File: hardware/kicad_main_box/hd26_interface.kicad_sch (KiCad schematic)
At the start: 1 part, among them J1 HD26_FEMALE

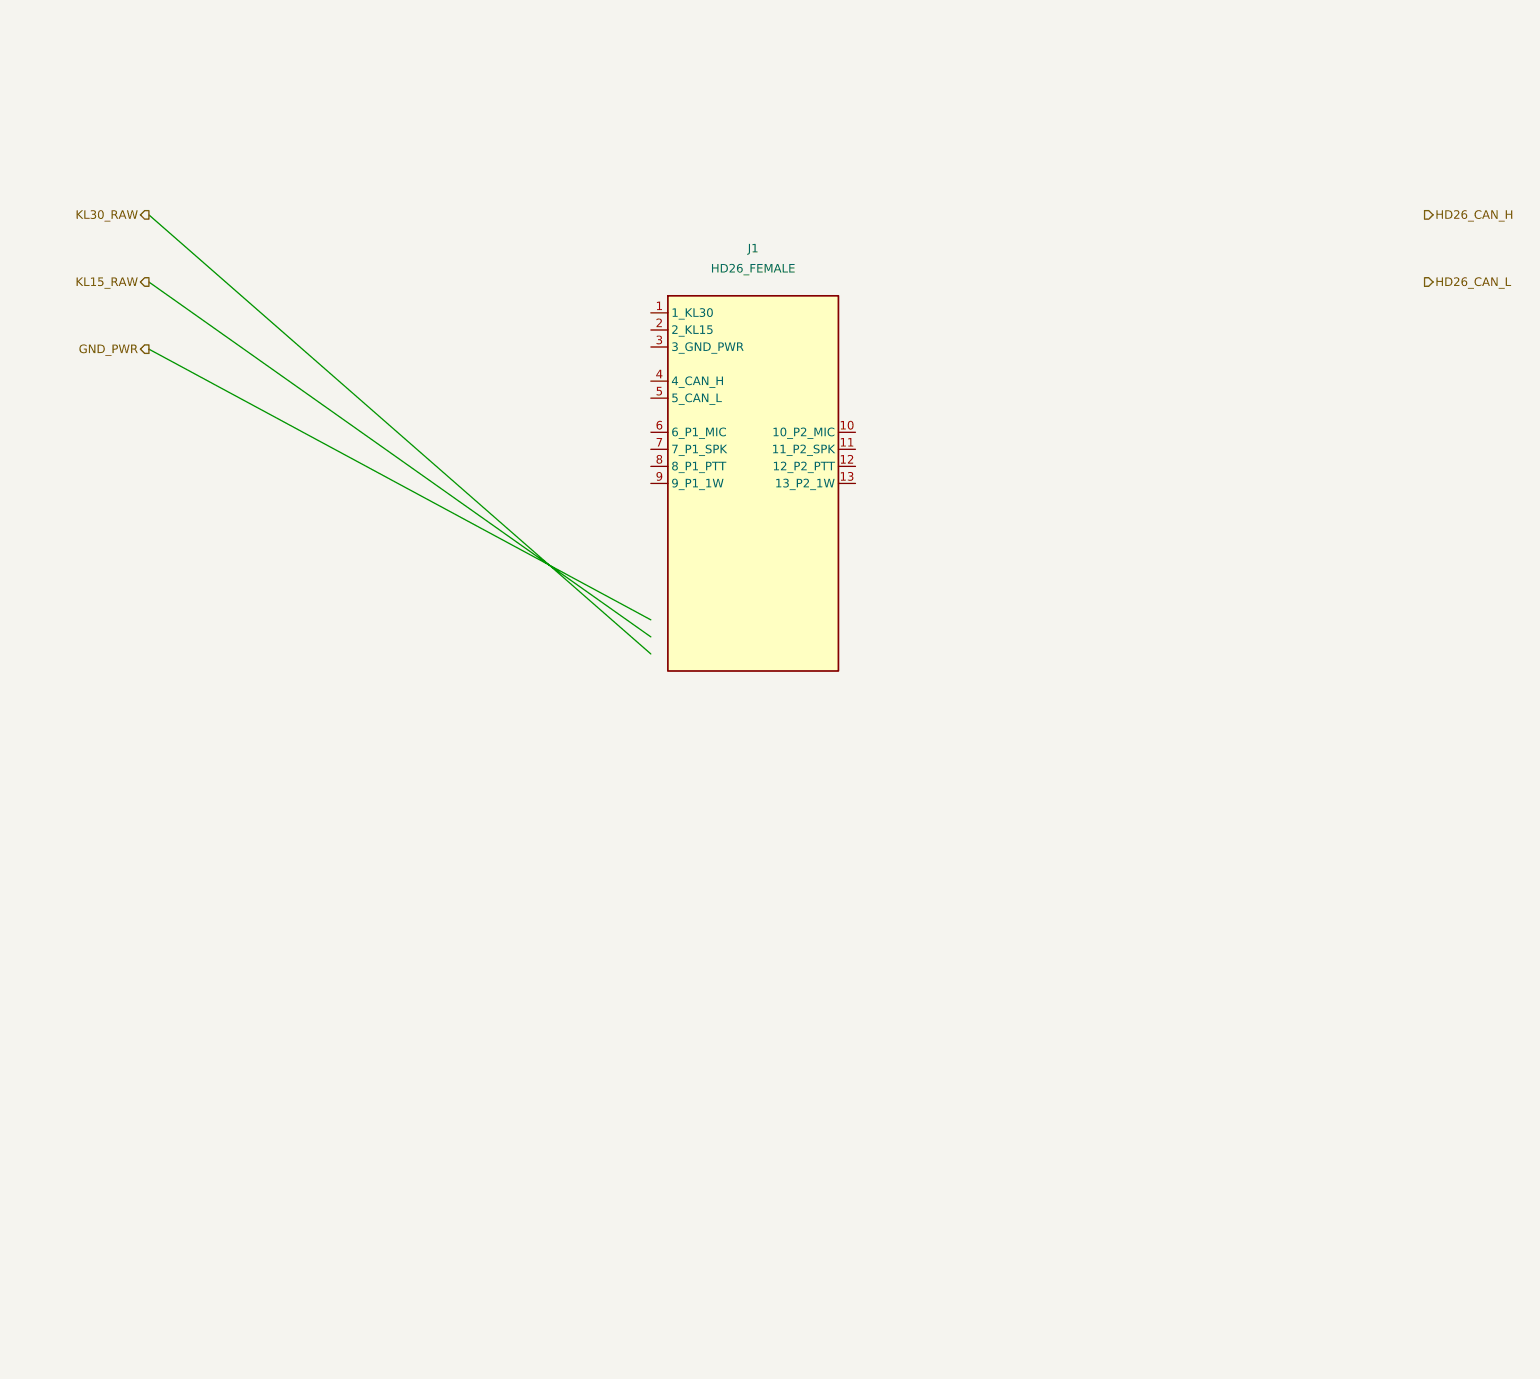
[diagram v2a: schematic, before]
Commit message: fix(kicad): Synchronize hierarchical sheet pins with child hierarchical labels across all sub-schematics
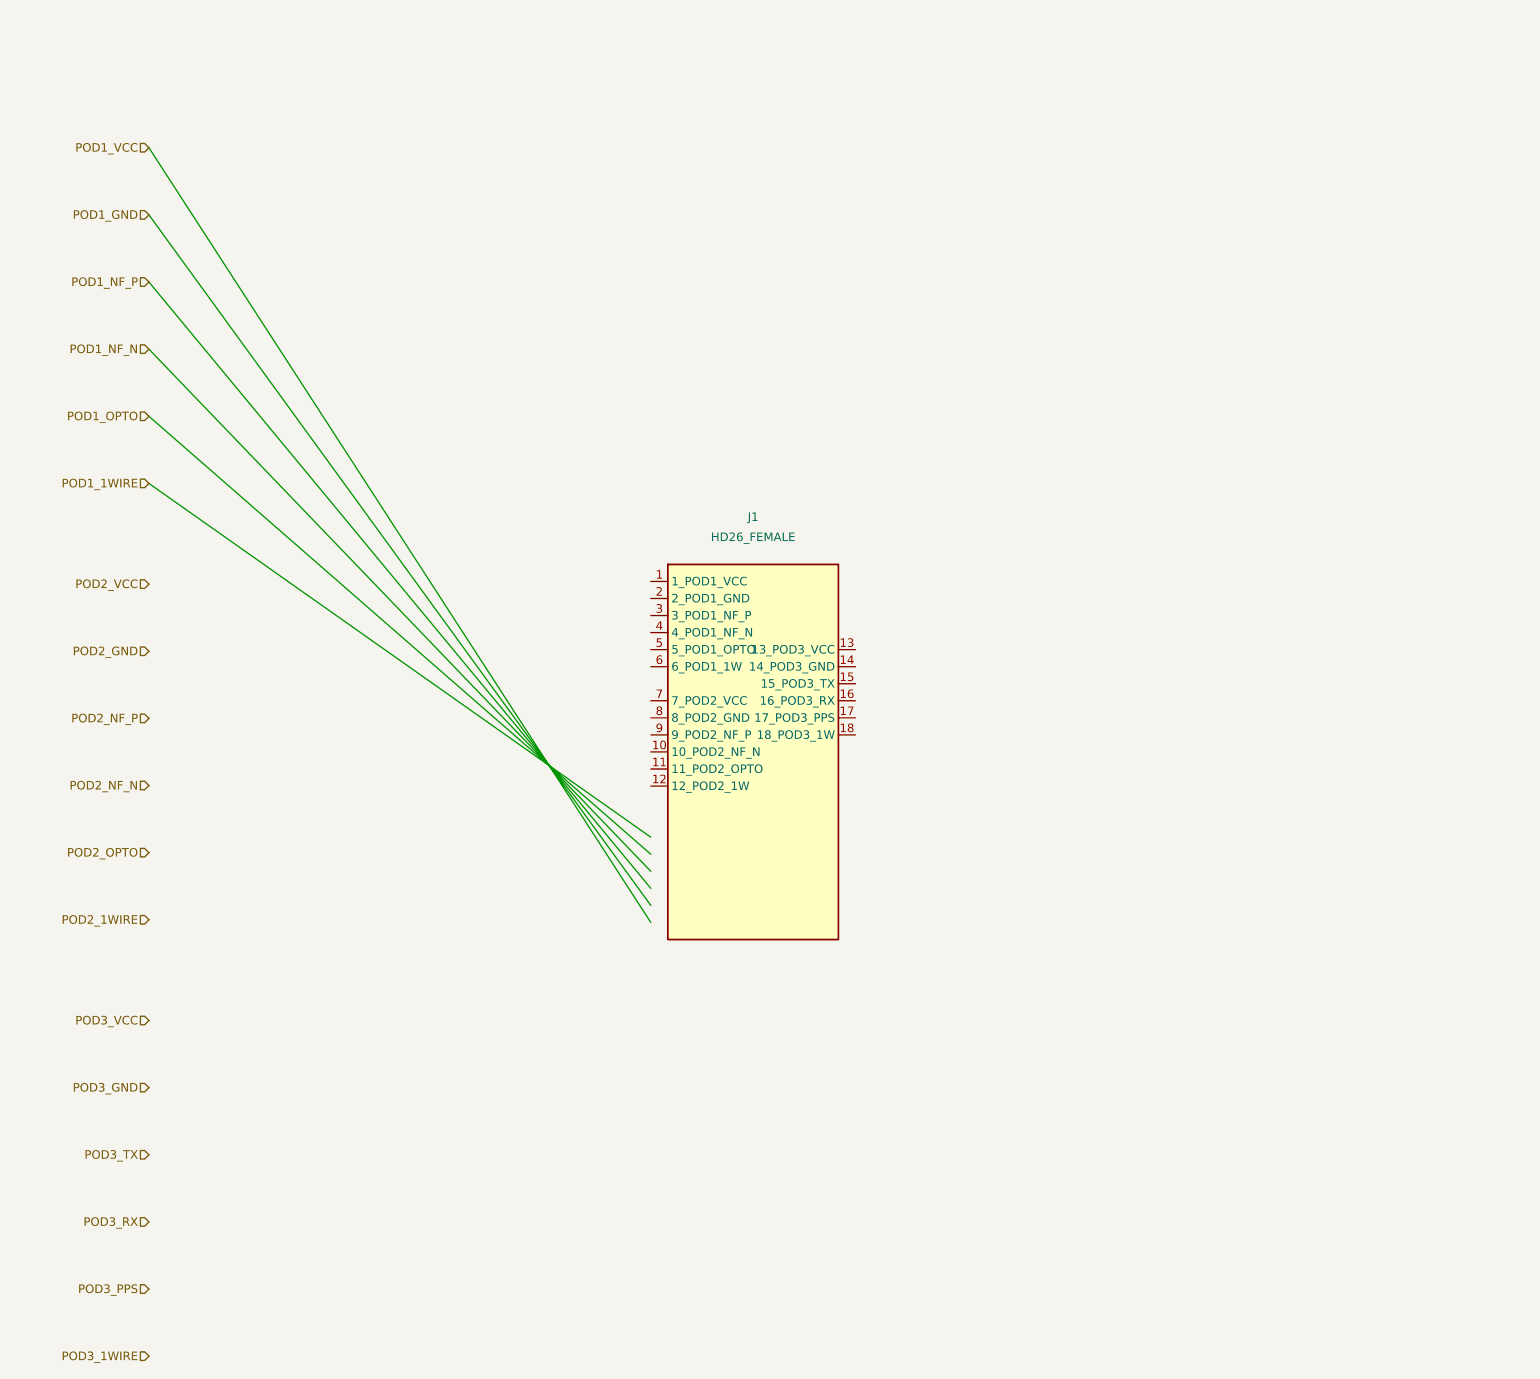
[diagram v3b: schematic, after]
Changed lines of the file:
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@@
 	)
 	;; =========================================================================
-	;; Hierarchical Labels
+	;; Hierarchical Labels (Matching Parent Sheet Pins exactly)
 	;; =========================================================================
-	(hierarchical_label "KL30_RAW" (shape output) (at 30.0 50.0 180) (effects (font (size 1.27 1.27)) (justify right)))
-	(hierarchical_label "KL15_RAW" (shape output) (at 30.0 60.0 180) (effects (font (size 1.27 1.27)) (justify right)))
-	(hierarchical_label "GND_PWR" (shape output) (at 30.0 70.0 180) (effects (font (size 1.27 1.27)) (justify right)))
-	(hierarchical_label "HD26_CAN_H" (shape output) (at 220.0 50.0 0) (effects (font (size 1.27 1.27)) (justify left)))
-	(hierarchical_label "HD26_CAN_L" (shape output) (at 220.0 60.0 0) (effects (font (size 1.27 1.27)) (justify left)))
+	(hierarchical_label "POD1_VCC" (shape input) (at 30.0 40.0 180) (effects (font (size 1.27 1.27)) (justify right)))
+	(hierarchical_label "POD1_GND" (shape input) (at 30.0 50.0 180) (effects (font (size 1.27 1.27)) (justify right)))
+	(hierarchical_label "POD1_NF_P" (shape input) (at 30.0 60.0 180) (effects (font (size 1.27 1.27)) (justify right)))
+	(hierarchical_label "POD1_NF_N" (shape input) (at 30.0 70.0 180) (effects (font (size 1.27 1.27)) (justify right)))
+	(hierarchical_label "POD1_OPTO" (shape input) (at 30.0 80.0 180) (effects (font (size 1.27 1.27)) (justify right)))
+	(hierarchical_label "POD1_1WIRE" (shape input) (at 30.0 90.0 180) (effects (font (size 1.27 1.27)) (justify right)))
+	(hierarchical_label "POD2_VCC" (shape input) (at 30.0 105.0 180) (effects (font (size 1.27 1.27)) (justify right)))
+	(hierarchical_label "POD2_GND" (shape input) (at 30.0 115.0 180) (effects (font (size 1.27 1.27)) (justify right)))
+	(hierarchical_label "POD2_NF_P" (shape input) (at 30.0 125.0 180) (effects (font (size 1.27 1.27)) (justify right)))
+	(hierarchical_label "POD2_NF_N" (shape input) (at 30.0 135.0 180) (effects (font (size 1.27 1.27)) (justify right)))
+	(hierarchical_label "POD2_OPTO" (shape input) (at 30.0 145.0 180) (effects (font (size 1.27 1.27)) (justify right)))
+	(hierarchical_label "POD2_1WIRE" (shape input) (at 30.0 155.0 180) (effects (font (size 1.27 1.27)) (justify right)))
+	(hierarchical_label "POD3_VCC" (shape input) (at 30.0 170.0 180) (effects (font (size 1.27 1.27)) (justify right)))
+	(hierarchical_label "POD3_GND" (shape input) (at 30.0 180.0 180) (effects (font (size 1.27 1.27)) (justify right)))
+	(hierarchical_label "POD3_TX" (shape input) (at 30.0 190.0 180) (effects (font (size 1.27 1.27)) (justify right)))
+	(hierarchical_label "POD3_RX" (shape input) (at 30.0 200.0 180) (effects (font (size 1.27 1.27)) (justify right)))
+	(hierarchical_label "POD3_PPS" (shape input) (at 30.0 210.0 180) (effects (font (size 1.27 1.27)) (justify right)))
+	(hierarchical_label "POD3_1WIRE" (shape input) (at 30.0 220.0 180) (effects (font (size 1.27 1.27)) (justify right)))
 	;; =========================================================================
 	;; Symbols Placement
 	;; =========================================================================
 	;; J1: HD26 High Density Female D-Sub
-	(symbol (lib_id "Connector:HD26_Female") (at 120.0 90.0 0) (unit 1)
+	(symbol (lib_id "Connector:HD26_Female") (at 120.0 130.0 0) (unit 1)
 		(in_bom yes) (on_board yes) (dnp no)
-		(property "Reference" "J1" (at 120.0 55.0 0) (effects (font (size 1.27 1.27))))
-		(property "Value" "HD26_FEMALE" (at 120.0 58.0 0) (effects (font (size 1.27 1.27))))
+		(property "Reference" "J1" (at 120.0 95.0 0) (effects (font (size 1.27 1.27))))
+		(property "Value" "HD26_FEMALE" (at 120.0 98.0 0) (effects (font (size 1.27 1.27))))
 		(pin "1")
 		(pin "2")
@@
 		(pin "12")
 		(pin "13")
+		(pin "14")
+		(pin "15")
+		(pin "16")
+		(pin "17")
+		(pin "18")
 	)
 	;; Wires
-	(wire (pts (xy 30.0 50.0) (xy 104.76 115.4)) (stroke (width 0) (type solid)))
-	(wire (pts (xy 30.0 60.0) (xy 104.76 112.86)) (stroke (width 0) (type solid)))
-	(wire (pts (xy 30.0 70.0) (xy 104.76 110.32)) (stroke (width 0) (type solid)))
+	(wire (pts (xy 30.0 40.0) (xy 104.76 155.4)) (stroke (width 0) (type solid)))
+	(wire (pts (xy 30.0 50.0) (xy 104.76 152.86)) (stroke (width 0) (type solid)))
+	(wire (pts (xy 30.0 60.0) (xy 104.76 150.32)) (stroke (width 0) (type solid)))
+	(wire (pts (xy 30.0 70.0) (xy 104.76 147.78)) (stroke (width 0) (type solid)))
+	(wire (pts (xy 30.0 80.0) (xy 104.76 145.24)) (stroke (width 0) (type solid)))
+	(wire (pts (xy 30.0 90.0) (xy 104.76 142.7)) (stroke (width 0) (type solid)))
 )
